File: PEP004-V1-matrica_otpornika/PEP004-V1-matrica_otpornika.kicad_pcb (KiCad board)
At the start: 2 copper layers, 90 x 45 mm, 39 parts, among them J1 Screw_Terminal_01x02, SW1 SW_Push, SW10 SW_Push, SW11 SW_Push, SW12 SW_Push, SW13 SW_Push, SW14 SW_Push, SW15 SW_Push, SW16 SW_Push, SW2 SW_Push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

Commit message: Update 1,2,3,4,5,7, lib.
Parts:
- added G***: LOGO, PEP_library:petnica_logo, F.Cu at (112.7, 93.2)
- R6: value 1K -> 1k
- moved REF** 22.4 mm to (122.2, 93.2)
- moved J1 1.10 mm to (113.8, 80.2)
- moved REF** 0.30 mm to (174.1, 103.5)
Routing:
- net 9V: track 43.5 -> 42.4 mm
- net 0: track 72.5 -> 71.4 mm, vias 0 -> 1
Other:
- board text added: "D1"
- board text added: "R1"
- board text added: "R2"
- board text added: "R3"
- board text added: "R4"
- board text added: "R5"
- board text added: "R6"
- board text added: "R7"
- board text added: "R8"

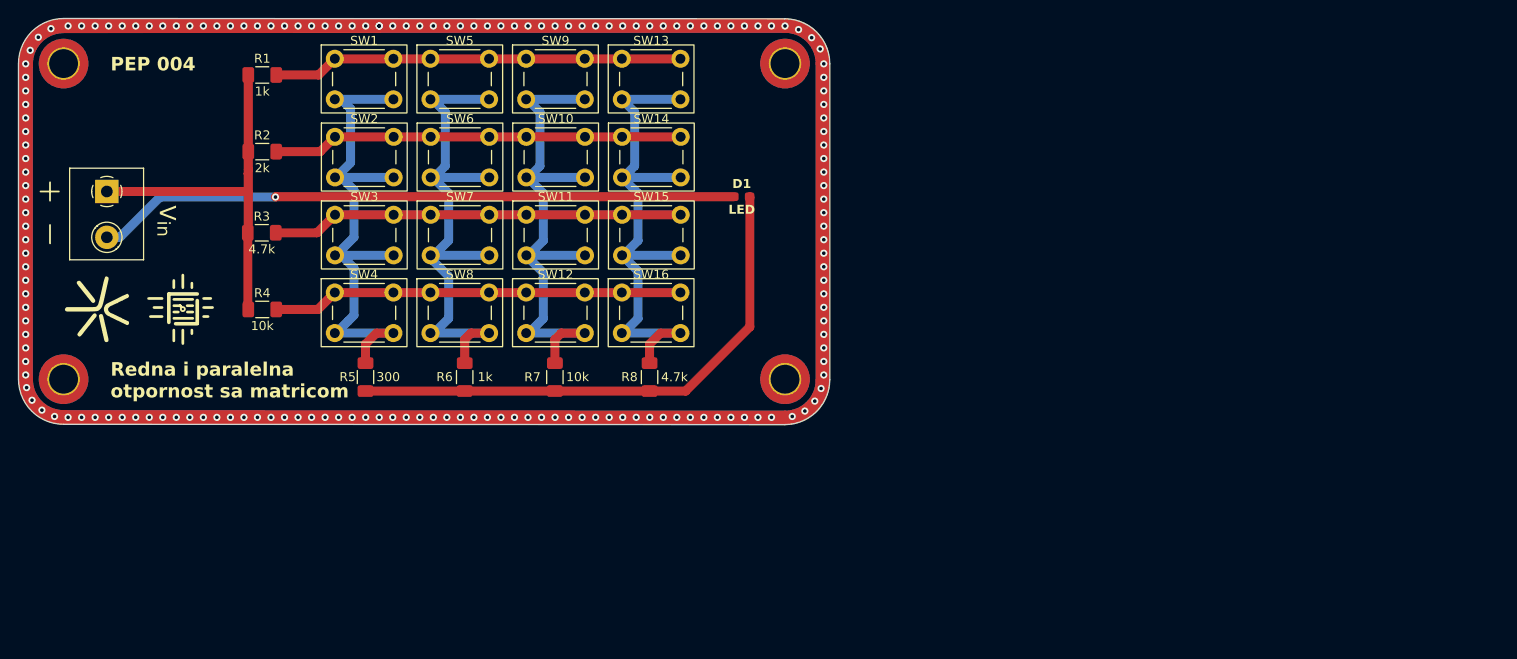
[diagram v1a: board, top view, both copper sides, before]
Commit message: Library moved, PEP004 placement needed.
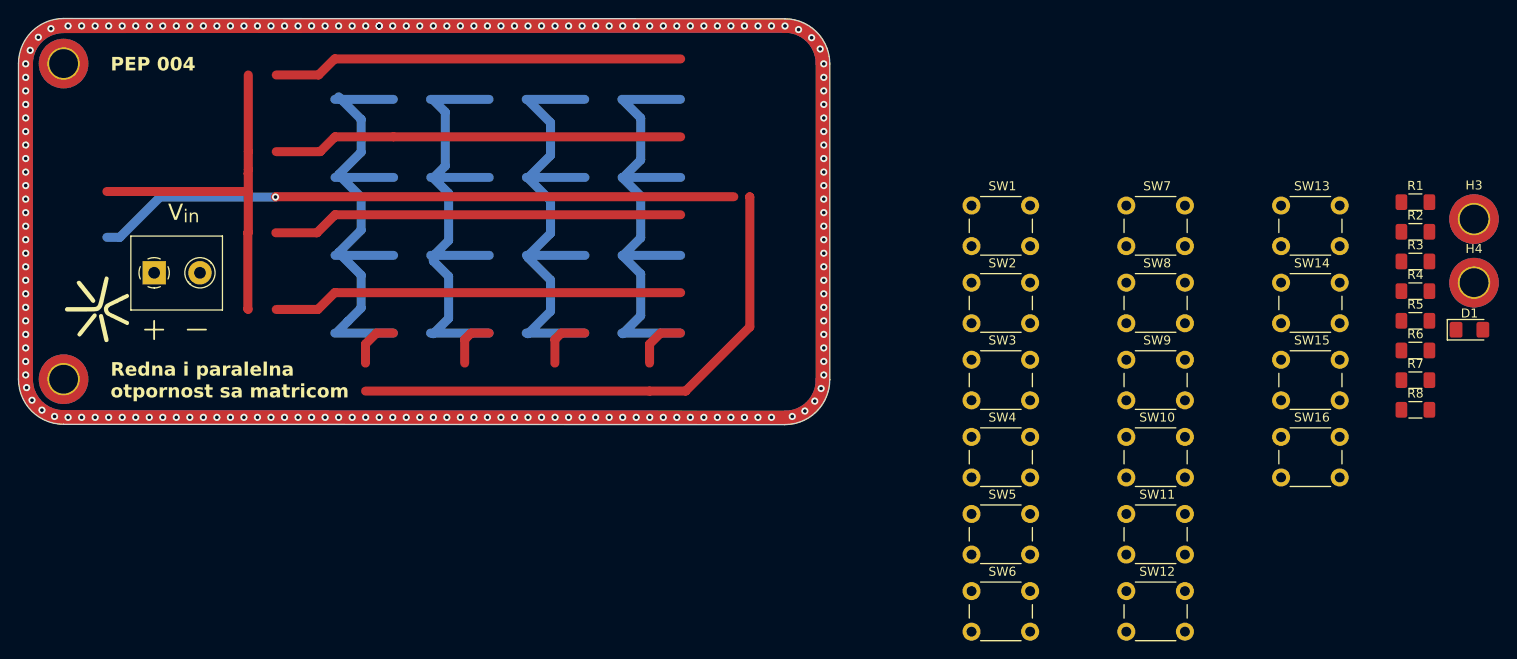
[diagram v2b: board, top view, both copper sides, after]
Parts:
- removed REF** (x8): R_silk_symbol, PEP_library:R_silk_symbol
- removed REF**: ele_petnica_logo, PEP_library:ele_petnica_logo
- D1: footprint LED_SMD:LED_0603_1608Metric_Pad1.05x0.95mm_HandSolder -> LED_SMD:LED_1206_3216Metric_Pad1.42x1.75mm_HandSolder
- J1: footprint PEP_library:TerminalBlock_Phoenix_MKDS-1,5-2-5.08_1x02_P5.08mm_Horizontal -> PEP library:TerminalBlock_Phoenix_MKDS-1,5-2-5.08_1x02_P5.08mm_Horizontal
- R1, R4, R8: footprint PEP_library:R_smd -> Resistor_SMD:R_1206_3216Metric_Pad1.30x1.75mm_HandSolder
- R2: value 2k -> 2.2k; footprint PEP_library:R_smd -> Resistor_SMD:R_1206_3216Metric_Pad1.30x1.75mm_HandSolder
- R3: value 4.7k -> 22k; footprint PEP_library:R_smd -> Resistor_SMD:R_1206_3216Metric_Pad1.30x1.75mm_HandSolder
- R5: value 300 -> 220; footprint PEP_library:R_smd -> Resistor_SMD:R_1206_3216Metric_Pad1.30x1.75mm_HandSolder
- R6: value 1k -> 100k; footprint PEP_library:R_smd -> Resistor_SMD:R_1206_3216Metric_Pad1.30x1.75mm_HandSolder
- R7: value 10k -> 47k; footprint PEP_library:R_smd -> Resistor_SMD:R_1206_3216Metric_Pad1.30x1.75mm_HandSolder
- SW1, SW10, SW11, SW12, SW13, SW14, SW15, SW16, SW2, SW3, SW4, SW5, SW6, SW7, SW8, SW9: footprint PEP_library:SW_PUSH_6mm_H4.3mm -> PEP library:SW_PUSH_6mm_H4.3mm
- moved R1 128.6 mm to (258.9, 81.4)
- moved R2 128.2 mm to (258.9, 84.7)
- moved R3 128.0 mm to (258.9, 87.9)
- moved R4 127.9 mm to (258.9, 91.2)
- moved R5 116.6 mm to (258.9, 94.5), turned to 0 degrees
- moved R6 105.5 mm to (258.9, 97.8), turned to 0 degrees
- moved R7 95.4 mm to (258.9, 101.1), turned to 0 degrees
- moved R8 85.0 mm to (258.9, 104.4), turned to 0 degrees
- moved D1 82.0 mm to (264.9, 95.5)
- moved SW5 78.4 mm to (213.0, 118.3)
- moved H3 78.3 mm to (265.4, 83.2)
- moved SW6 78.3 mm to (213.0, 126.8)
- moved SW8 77.2 mm to (230.1, 92.6)
- moved H4 77.2 mm to (265.4, 90.3)
- moved SW7 77.1 mm to (230.1, 84.1)
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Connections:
- D1 pad 2: (no net) -> Net-(D1-A)
- R1 pad 2: (no net) -> Net-(R1-Pad2)
- R2 pad 2: (no net) -> Net-(R2-Pad2)
- R3 pad 2: (no net) -> Net-(R3-Pad2)
- R4 pad 2: (no net) -> Net-(R4-Pad2)
- R5 pad 1: (no net) -> Net-(D1-A)
- R5 pad 2: (no net) -> Net-(R5-Pad2)
- R6 pad 1: (no net) -> Net-(D1-A)
- R6 pad 2: (no net) -> Net-(R6-Pad2)
- R7 pad 1: (no net) -> Net-(D1-A)
- R7 pad 2: (no net) -> Net-(R7-Pad2)
- R8 pad 1: (no net) -> Net-(D1-A)
- R8 pad 2: (no net) -> Net-(R8-Pad2)
- SW1 pad 1: (no net) -> Net-(R1-Pad2)
- SW1 pad 2: (no net) -> Net-(R5-Pad2)
- SW10 pad 1: (no net) -> Net-(R2-Pad2)
- SW10 pad 2: (no net) -> Net-(R7-Pad2)
- SW11 pad 1: (no net) -> Net-(R3-Pad2)
- SW11 pad 2: (no net) -> Net-(R7-Pad2)
- SW12 pad 1: (no net) -> Net-(R4-Pad2)
- SW12 pad 2: (no net) -> Net-(R7-Pad2)
- SW13 pad 1: (no net) -> Net-(R1-Pad2)
- SW13 pad 2: (no net) -> Net-(R8-Pad2)
- SW14 pad 1: (no net) -> Net-(R2-Pad2)
- SW14 pad 2: (no net) -> Net-(R8-Pad2)
- SW15 pad 1: (no net) -> Net-(R3-Pad2)
- SW15 pad 2: (no net) -> Net-(R8-Pad2)
- SW16 pad 1: (no net) -> Net-(R4-Pad2)
- SW16 pad 2: (no net) -> Net-(R8-Pad2)
- SW2 pad 1: (no net) -> Net-(R2-Pad2)
- SW2 pad 2: (no net) -> Net-(R5-Pad2)
- SW3 pad 1: (no net) -> Net-(R3-Pad2)
- SW3 pad 2: (no net) -> Net-(R5-Pad2)
- SW4 pad 1: (no net) -> Net-(R4-Pad2)
- SW4 pad 2: (no net) -> Net-(R5-Pad2)
- SW5 pad 1: (no net) -> Net-(R1-Pad2)
- SW5 pad 2: (no net) -> Net-(R6-Pad2)
- SW6 pad 1: (no net) -> Net-(R2-Pad2)
- SW6 pad 2: (no net) -> Net-(R6-Pad2)
- SW7 pad 1: (no net) -> Net-(R3-Pad2)
- SW7 pad 2: (no net) -> Net-(R6-Pad2)
- SW8 pad 1: (no net) -> Net-(R4-Pad2)
- SW8 pad 2: (no net) -> Net-(R6-Pad2)
- SW9 pad 1: (no net) -> Net-(R1-Pad2)
- SW9 pad 2: (no net) -> Net-(R7-Pad2)
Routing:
- net (no net): track 492.2 -> 497.9 mm
